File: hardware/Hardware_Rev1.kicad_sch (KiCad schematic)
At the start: 160 parts, among them J1 RJ45_LED_Shielded, J2 6P6C, Q1 BSS138, Q10 AO3401A, Q11 AO3401A, Q12 AO3401A, Q13 BSS138, Q14 BSS138, Q15 BSS138, Q16 AO3401A, Q17 AO3401A, Q18 AO3401A, Q19 BSS138, Q2 BSS138, Q20 BSS138, Q21 BSS138, Q22 AO3401A, Q23 AO3401A, Q24 AO3401A, Q3 BSS138, Q4 AO3401A, Q5 AO3401A, Q6 AO3401A, Q7 BSS138, Q8 BSS138, Q9 BSS138, U1 OKI, U2 Teensy4.1_DEV-16771

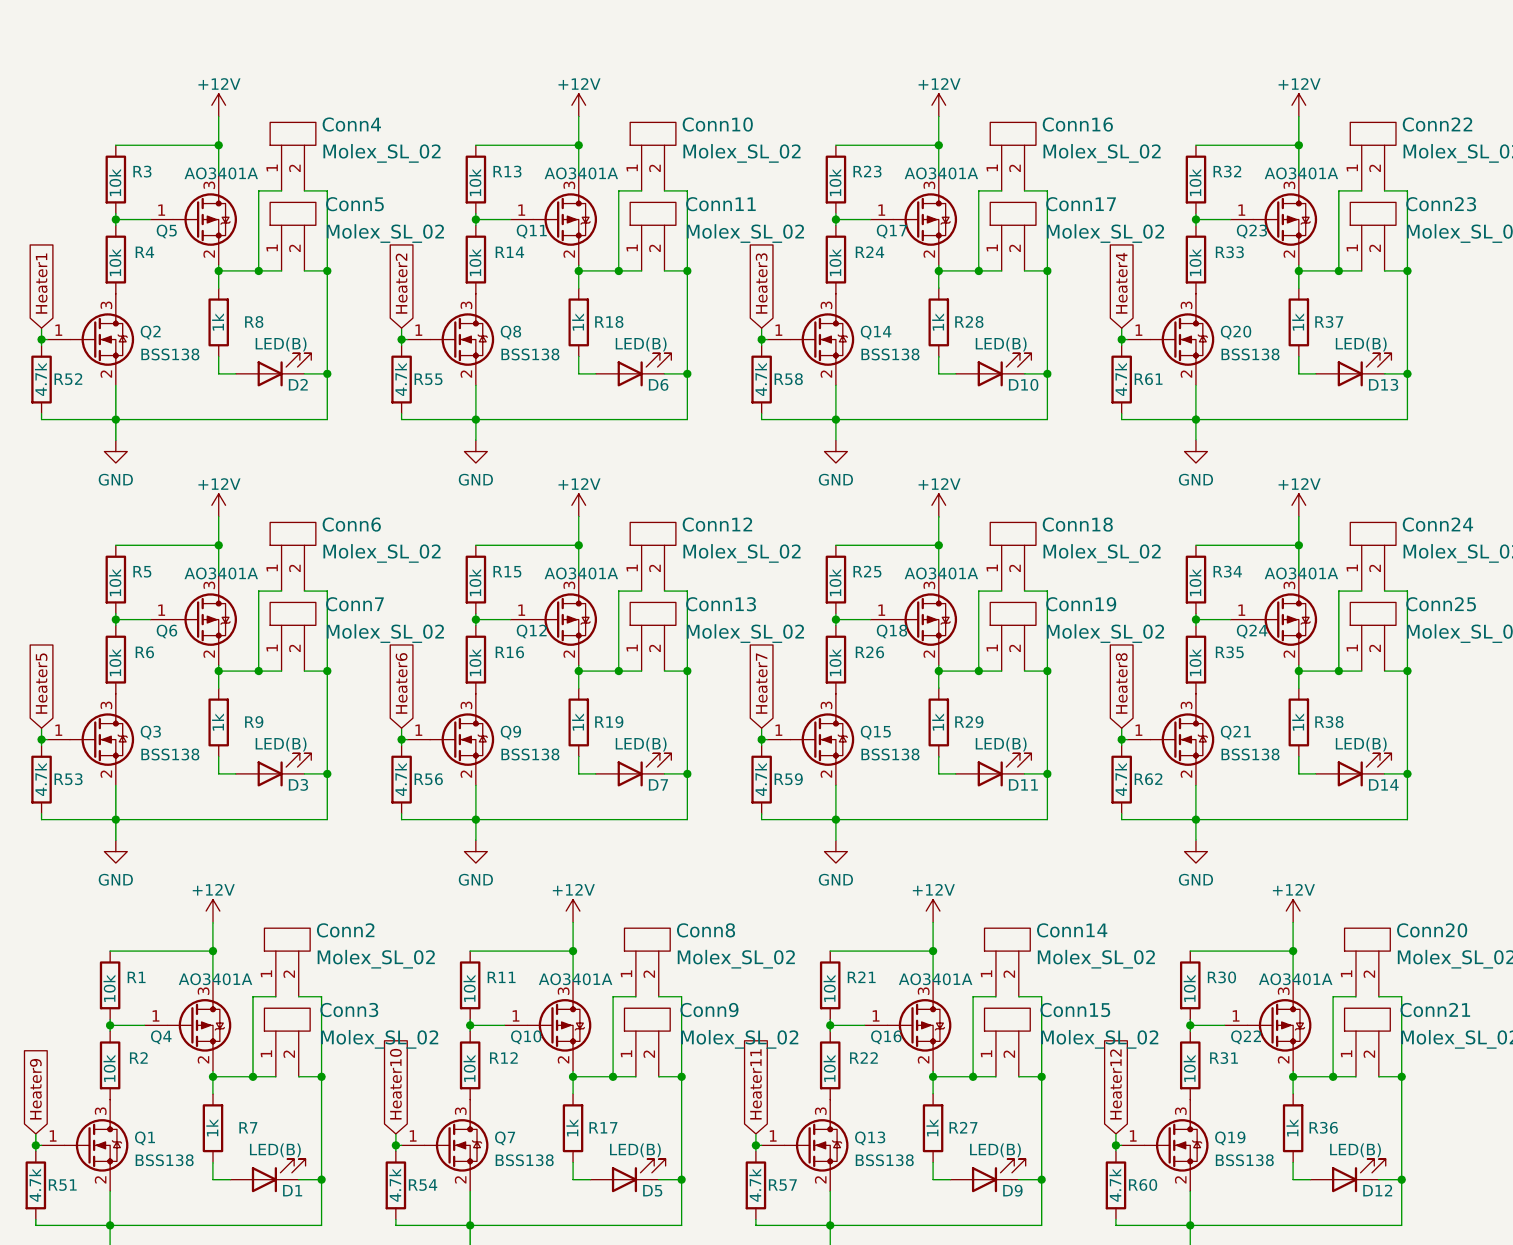
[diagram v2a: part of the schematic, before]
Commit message: Fixed schematic mosfets
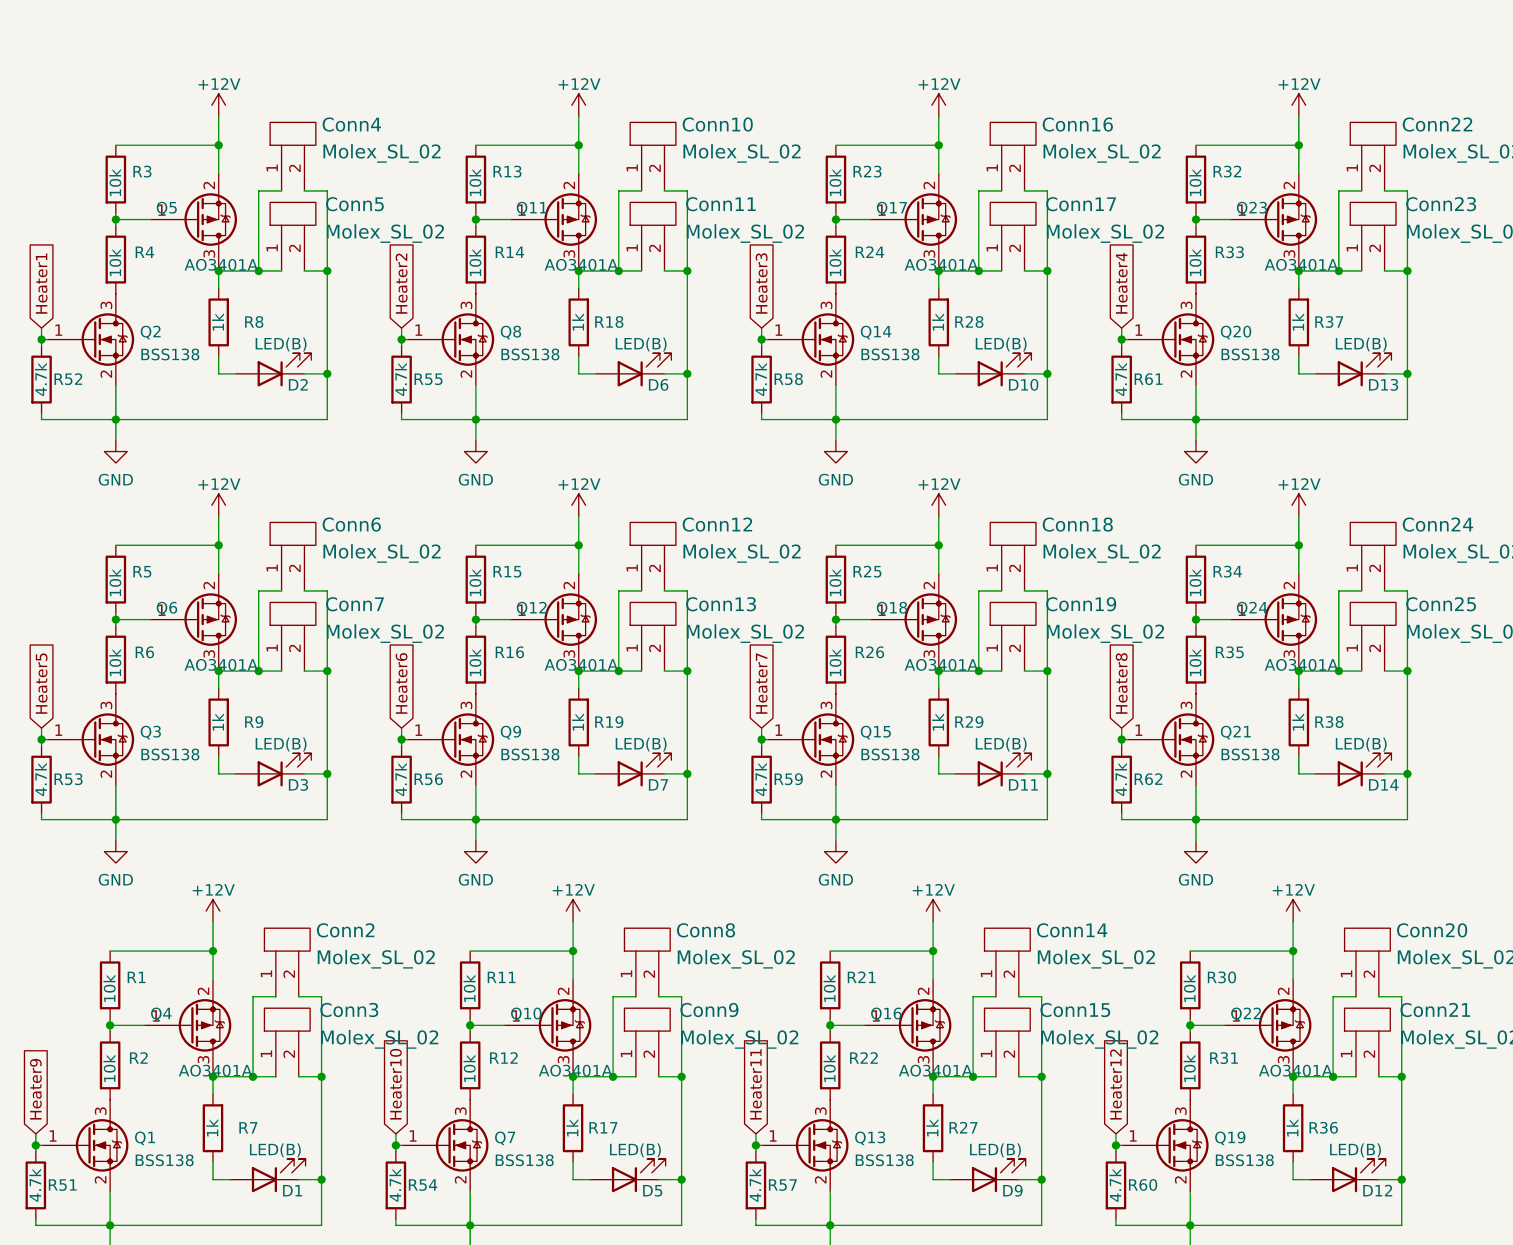
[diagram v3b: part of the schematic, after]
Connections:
- net +12V: now also Q10.2 (S), Q11.2 (S), Q12.2 (S), Q16.2 (S), Q17.2 (S), Q18.2 (S), Q22.2 (S), Q23.2 (S), Q24.2 (S), Q4.2 (S), Q5.2 (S), Q6.2 (S); no longer Q10.3 (D), Q11.3 (D), Q12.3 (D), Q16.3 (D), Q17.3 (D), Q18.3 (D), Q22.3 (D), Q23.3 (D), Q24.3 (D), Q4.3 (D), Q5.3 (D), Q6.3 (D)
- net at Conn20.1, Conn21.1, R36.2: now also Q22.3 (D); no longer Q22.2 (S)
- net at Conn22.1, Conn23.1, R37.2: now also Q23.3 (D); no longer Q23.2 (S)
- net at Conn8.1, Conn9.1, R17.2: now also Q10.3 (D); no longer Q10.2 (S)
- net at Conn4.1, Conn5.1, R8.2: now also Q5.3 (D); no longer Q5.2 (S)
- net at Conn14.1, Conn15.1, R27.2: now also Q16.3 (D); no longer Q16.2 (S)
- net at Conn6.1, Conn7.1, R9.2: now also Q6.3 (D); no longer Q6.2 (S)
- net at Conn12.1, Conn13.1, R19.2: now also Q12.3 (D); no longer Q12.2 (S)
- net at Conn16.1, Conn17.1, R28.2: now also Q17.3 (D); no longer Q17.2 (S)
- net at Conn24.1, Conn25.1, R38.2: now also Q24.3 (D); no longer Q24.2 (S)
- net at Conn10.1, Conn11.1, R18.2: now also Q11.3 (D); no longer Q11.2 (S)
- net at Conn2.1, Conn3.1, R7.2: now also Q4.3 (D); no longer Q4.2 (S)
- net at Conn18.1, Conn19.1, R29.2: now also Q18.3 (D); no longer Q18.2 (S)
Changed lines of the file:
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@@
     (pin "2")
   )
-  (symbol (lib_id "Transistor_FET:AO3401A") (at 150.495 161.29 0) (unit 1)
+  (symbol (lib_id "Transistor_FET:AO3401A") (at 150.495 161.29 0) (mirror x) (unit 1)
     (in_bom yes) (on_board yes)
-    (property "Reference" "Q22" (id 0) (at 146.05 162.56 0)
+    (property "Reference" "Q22" (id 0) (at 146.05 160.02 0)
       (effects (font (size 1.27 1.27)) (justify left))
     )
-    (property "Value" "AO3401A" (id 1) (at 149.225 156.21 0)
+    (property "Value" "AO3401A" (id 1) (at 149.225 166.37 0)
       (effects (font (size 1.27 1.27)) (justify left))
     )
-    (property "Footprint" "Package_TO_SOT_SMD:SOT-23" (id 2) (at 155.575 163.195 0)
+    (property "Footprint" "Package_TO_SOT_SMD:SOT-23" (id 2) (at 155.575 159.385 0)
       (effects (font (size 1.27 1.27) italic) (justify left) hide)
     )
@@
     (pin "3")
   )
-  (symbol (lib_id "Transistor_FET:AO3401A") (at 31.115 71.755 0) (unit 1)
+  (symbol (lib_id "Transistor_FET:AO3401A") (at 31.115 71.755 0) (mirror x) (unit 1)
     (in_bom yes) (on_board yes)
-    (property "Reference" "Q5" (id 0) (at 26.67 73.025 0)
+    (property "Reference" "Q5" (id 0) (at 26.67 70.485 0)
       (effects (font (size 1.27 1.27)) (justify left))
     )
-    (property "Value" "AO3401A" (id 1) (at 29.845 66.675 0)
+    (property "Value" "AO3401A" (id 1) (at 29.845 76.835 0)
       (effects (font (size 1.27 1.27)) (justify left))
     )
-    (property "Footprint" "Package_TO_SOT_SMD:SOT-23" (id 2) (at 36.195 73.66 0)
+    (property "Footprint" "Package_TO_SOT_SMD:SOT-23" (id 2) (at 36.195 69.85 0)
       (effects (font (size 1.27 1.27) italic) (justify left) hide)
     )
@@
     (pin "1")
   )
-  (symbol (lib_id "Transistor_FET:AO3401A") (at 31.115 116.205 0) (unit 1)
+  (symbol (lib_id "Transistor_FET:AO3401A") (at 31.115 116.205 0) (mirror x) (unit 1)
     (in_bom yes) (on_board yes)
-    (property "Reference" "Q6" (id 0) (at 26.67 117.475 0)
+    (property "Reference" "Q6" (id 0) (at 26.67 114.935 0)
       (effects (font (size 1.27 1.27)) (justify left))
     )
-    (property "Value" "AO3401A" (id 1) (at 29.845 111.125 0)
+    (property "Value" "AO3401A" (id 1) (at 29.845 121.285 0)
       (effects (font (size 1.27 1.27)) (justify left))
     )
-    (property "Footprint" "Package_TO_SOT_SMD:SOT-23" (id 2) (at 36.195 118.11 0)
+    (property "Footprint" "Package_TO_SOT_SMD:SOT-23" (id 2) (at 36.195 114.3 0)
       (effects (font (size 1.27 1.27) italic) (justify left) hide)
     )
@@
     (pin "2")
   )
-  (symbol (lib_id "Transistor_FET:AO3401A") (at 111.125 71.755 0) (unit 1)
+  (symbol (lib_id "Transistor_FET:AO3401A") (at 111.125 71.755 0) (mirror x) (unit 1)
     (in_bom yes) (on_board yes)
-    (property "Reference" "Q17" (id 0) (at 106.68 73.025 0)
+    (property "Reference" "Q17" (id 0) (at 106.68 70.485 0)
       (effects (font (size 1.27 1.27)) (justify left))
     )
-    (property "Value" "AO3401A" (id 1) (at 109.855 66.675 0)
+    (property "Value" "AO3401A" (id 1) (at 109.855 76.835 0)
       (effects (font (size 1.27 1.27)) (justify left))
     )
-    (property "Footprint" "Package_TO_SOT_SMD:SOT-23" (id 2) (at 116.205 73.66 0)
+    (property "Footprint" "Package_TO_SOT_SMD:SOT-23" (id 2) (at 116.205 69.85 0)
       (effects (font (size 1.27 1.27) italic) (justify left) hide)
     )
@@
     (pin "2")
   )
-  (symbol (lib_id "Transistor_FET:AO3401A") (at 110.49 161.29 0) (unit 1)
+  (symbol (lib_id "Transistor_FET:AO3401A") (at 110.49 161.29 0) (mirror x) (unit 1)
     (in_bom yes) (on_board yes)
-    (property "Reference" "Q16" (id 0) (at 106.045 162.56 0)
+    (property "Reference" "Q16" (id 0) (at 106.045 160.02 0)
       (effects (font (size 1.27 1.27)) (justify left))
     )
-    (property "Value" "AO3401A" (id 1) (at 109.22 156.21 0)
+    (property "Value" "AO3401A" (id 1) (at 109.22 166.37 0)
       (effects (font (size 1.27 1.27)) (justify left))
     )
-    (property "Footprint" "Package_TO_SOT_SMD:SOT-23" (id 2) (at 115.57 163.195 0)
+    (property "Footprint" "Package_TO_SOT_SMD:SOT-23" (id 2) (at 115.57 159.385 0)
       (effects (font (size 1.27 1.27) italic) (justify left) hide)
     )
@@
     (pin "2")
   )
-  (symbol (lib_id "Transistor_FET:AO3401A") (at 151.13 116.205 0) (unit 1)
+  (symbol (lib_id "Transistor_FET:AO3401A") (at 151.13 116.205 0) (mirror x) (unit 1)
     (in_bom yes) (on_board yes)
-    (property "Reference" "Q24" (id 0) (at 146.685 117.475 0)
+    (property "Reference" "Q24" (id 0) (at 146.685 114.935 0)
       (effects (font (size 1.27 1.27)) (justify left))
     )
-    (property "Value" "AO3401A" (id 1) (at 149.86 111.125 0)
+    (property "Value" "AO3401A" (id 1) (at 149.86 121.285 0)
       (effects (font (size 1.27 1.27)) (justify left))
     )
-    (property "Footprint" "Package_TO_SOT_SMD:SOT-23" (id 2) (at 156.21 118.11 0)
+    (property "Footprint" "Package_TO_SOT_SMD:SOT-23" (id 2) (at 156.21 114.3 0)
       (effects (font (size 1.27 1.27) italic) (justify left) hide)
     )
@@
     (pin "2")
   )
-  (symbol (lib_id "Transistor_FET:AO3401A") (at 70.485 161.29 0) (unit 1)
+  (symbol (lib_id "Transistor_FET:AO3401A") (at 70.485 161.29 0) (mirror x) (unit 1)
     (in_bom yes) (on_board yes)
-    (property "Reference" "Q10" (id 0) (at 66.04 162.56 0)
+    (property "Reference" "Q10" (id 0) (at 66.04 160.02 0)
       (effects (font (size 1.27 1.27)) (justify left))
     )
-    (property "Value" "AO3401A" (id 1) (at 69.215 156.21 0)
+    (property "Value" "AO3401A" (id 1) (at 69.215 166.37 0)
       (effects (font (size 1.27 1.27)) (justify left))
     )
-    (property "Footprint" "Package_TO_SOT_SMD:SOT-23" (id 2) (at 75.565 163.195 0)
+    (property "Footprint" "Package_TO_SOT_SMD:SOT-23" (id 2) (at 75.565 159.385 0)
       (effects (font (size 1.27 1.27) italic) (justify left) hide)
     )
@@
     (pin "3")
   )
-  (symbol (lib_id "Transistor_FET:AO3401A") (at 71.12 116.205 0) (unit 1)
+  (symbol (lib_id "Transistor_FET:AO3401A") (at 71.12 116.205 0) (mirror x) (unit 1)
     (in_bom yes) (on_board yes)
-    (property "Reference" "Q12" (id 0) (at 66.675 117.475 0)
+    (property "Reference" "Q12" (id 0) (at 66.675 114.935 0)
       (effects (font (size 1.27 1.27)) (justify left))
     )
-    (property "Value" "AO3401A" (id 1) (at 69.85 111.125 0)
+    (property "Value" "AO3401A" (id 1) (at 69.85 121.285 0)
       (effects (font (size 1.27 1.27)) (justify left))
     )
-    (property "Footprint" "Package_TO_SOT_SMD:SOT-23" (id 2) (at 76.2 118.11 0)
+    (property "Footprint" "Package_TO_SOT_SMD:SOT-23" (id 2) (at 76.2 114.3 0)
       (effects (font (size 1.27 1.27) italic) (justify left) hide)
     )
@@
     (pin "1")
   )
-  (symbol (lib_id "Transistor_FET:AO3401A") (at 30.48 161.29 0) (unit 1)
+  (symbol (lib_id "Transistor_FET:AO3401A") (at 30.48 161.29 0) (mirror x) (unit 1)
     (in_bom yes) (on_board yes)
-    (property "Reference" "Q4" (id 0) (at 26.035 162.56 0)
+    (property "Reference" "Q4" (id 0) (at 26.035 160.02 0)
       (effects (font (size 1.27 1.27)) (justify left))
     )
-    (property "Value" "AO3401A" (id 1) (at 29.21 156.21 0)
+    (property "Value" "AO3401A" (id 1) (at 29.21 166.37 0)
       (effects (font (size 1.27 1.27)) (justify left))
     )
-    (property "Footprint" "Package_TO_SOT_SMD:SOT-23" (id 2) (at 35.56 163.195 0)
+    (property "Footprint" "Package_TO_SOT_SMD:SOT-23" (id 2) (at 35.56 159.385 0)
       (effects (font (size 1.27 1.27) italic) (justify left) hide)
     )
@@
     (pin "3")
   )
-  (symbol (lib_id "Transistor_FET:AO3401A") (at 111.125 116.205 0) (unit 1)
+  (symbol (lib_id "Transistor_FET:AO3401A") (at 111.125 116.205 0) (mirror x) (unit 1)
     (in_bom yes) (on_board yes)
-    (property "Reference" "Q18" (id 0) (at 106.68 117.475 0)
+    (property "Reference" "Q18" (id 0) (at 106.68 114.935 0)
       (effects (font (size 1.27 1.27)) (justify left))
     )
-    (property "Value" "AO3401A" (id 1) (at 109.855 111.125 0)
+    (property "Value" "AO3401A" (id 1) (at 109.855 121.285 0)
       (effects (font (size 1.27 1.27)) (justify left))
     )
-    (property "Footprint" "Package_TO_SOT_SMD:SOT-23" (id 2) (at 116.205 118.11 0)
+    (property "Footprint" "Package_TO_SOT_SMD:SOT-23" (id 2) (at 116.205 114.3 0)
       (effects (font (size 1.27 1.27) italic) (justify left) hide)
     )
@@
     (pin "2")
   )
-  (symbol (lib_id "Transistor_FET:AO3401A") (at 71.12 71.755 0) (unit 1)
+  (symbol (lib_id "Transistor_FET:AO3401A") (at 71.12 71.755 0) (mirror x) (unit 1)
     (in_bom yes) (on_board yes)
-    (property "Reference" "Q11" (id 0) (at 66.675 73.025 0)
+    (property "Reference" "Q11" (id 0) (at 66.675 70.485 0)
       (effects (font (size 1.27 1.27)) (justify left))
     )
-    (property "Value" "AO3401A" (id 1) (at 69.85 66.675 0)
+    (property "Value" "AO3401A" (id 1) (at 69.85 76.835 0)
       (effects (font (size 1.27 1.27)) (justify left))
     )
-    (property "Footprint" "Package_TO_SOT_SMD:SOT-23" (id 2) (at 76.2 73.66 0)
+    (property "Footprint" "Package_TO_SOT_SMD:SOT-23" (id 2) (at 76.2 69.85 0)
       (effects (font (size 1.27 1.27) italic) (justify left) hide)
     )
@@
     (pin "2")
   )
-  (symbol (lib_id "Transistor_FET:AO3401A") (at 151.13 71.755 0) (unit 1)
+  (symbol (lib_id "Transistor_FET:AO3401A") (at 151.13 71.755 0) (mirror x) (unit 1)
     (in_bom yes) (on_board yes)
-    (property "Reference" "Q23" (id 0) (at 146.685 73.025 0)
+    (property "Reference" "Q23" (id 0) (at 146.685 70.485 0)
       (effects (font (size 1.27 1.27)) (justify left))
     )
-    (property "Value" "AO3401A" (id 1) (at 149.86 66.675 0)
+    (property "Value" "AO3401A" (id 1) (at 149.86 76.835 0)
       (effects (font (size 1.27 1.27)) (justify left))
     )
-    (property "Footprint" "Package_TO_SOT_SMD:SOT-23" (id 2) (at 156.21 73.66 0)
+    (property "Footprint" "Package_TO_SOT_SMD:SOT-23" (id 2) (at 156.21 69.85 0)
       (effects (font (size 1.27 1.27) italic) (justify left) hide)
     )

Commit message: Rev2 schematic
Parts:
- removed Conn10, Conn11, Conn12, Conn13, Conn14, Conn15, Conn16, Conn17, Conn18, Conn19, Conn2, Conn20, Conn21, Conn22, Conn23, Conn24, Conn25, Conn3, Conn4, Conn5, Conn6, Conn7, Conn8, Conn9: Molex_SL_02, MRDT_Connectors:MOLEX_SL_02_Vertical, symbol MRDT_Connectors:Molex_SL_02
- removed J2: 6P6C, Connector_PinHeader_2.00mm:PinHeader_2x03_P2.00mm_Vertical, symbol Connector:6P6C
- removed Q10, Q11, Q12, Q16, Q17, Q18, Q22, Q23, Q24, Q4, Q5, Q6: AO3401A, Package_TO_SOT_SMD:SOT-23, symbol Transistor_FET:AO3401A
- added C4: 100uF, Capacitor_THT:CP_Radial_D6.3mm_P2.50mm, symbol Device:C_Polarized
- added C5: 220uF, Capacitor_THT:CP_Radial_D6.3mm_P2.50mm, symbol Device:C_Polarized
- added C6: 470uF, Capacitor_THT:CP_Radial_D10.0mm_P2.50mm, symbol Device:C_Polarized
- added Conn10, Conn11, Conn12, Conn13, Conn2, Conn3, Conn4, Conn5, Conn6, Conn7, Conn8, Conn9: AndersonPP, MRDT_Connectors:Square_Anderson_2_V_Side_By_Side, symbol MRDT_Connectors:AndersonPP
- added Q10, Q11, Q12, Q16, Q17, Q18, Q22, Q23, Q24, Q4, Q5, Q6: Q_PMOS_GSD, Package_TO_SOT_SMD:SOT-23-3, symbol Device:Q_PMOS_GSD
- U2: footprint MRDT_Shields:Teensy_4_1_Bare -> MRDT_Shields:Teensy_4_1_Ethernet
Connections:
- net RX+ is gone; now on net R+: J1.4
- net RX- is gone; now on net R-: J1.6
- net TX+ is gone; now on net T+: J1.1
- net TX- is gone; now on net T-: J1.3
- net +12V: now also C4.1, C5.1, C6.1, Q10.3 (D), Q11.3 (D), Q12.3 (D), Q16.3 (D), Q17.3 (D), Q18.3 (D), Q22.3 (D), Q23.3 (D), Q24.3 (D), Q4.3 (D), Q5.3 (D), Q6.3 (D)
- net GND: now also C3.2, J1.8, J1.9, C4.2, C5.2, C6.2, Conn10.1 (GND), Conn11.1 (GND), Conn12.1 (GND), Conn13.1 (GND), Conn2.1 (GND), Conn3.1 (GND), Conn4.1 (GND), Conn5.1 (GND), Conn6.1 (GND), Conn7.1 (GND), Conn8.1 (GND), Conn9.1 (GND)
- net at R34.2, R35.1: now also Q24.1 (G)
- net at R30.2, R31.1: now also Q22.1 (G)
- net at R36.2: now also Conn13.1, Q22.2 (S)
- net at R21.2, R22.1: now also Q17.1 (G)
- net Overheat2: now reaches R40.2, U2.8 (TX2)
- net LED: now reaches J1.10
- net LED: now also U2.LED
- net Overheat10: now reaches R48.2, U2.0 (RX1)
- net Overheat9: now reaches R47.2, U2.1 (TX1)
- net Overheat8: now reaches R46.2, U2.2 (OUT2)
- net Overheat11: now reaches R49.2, U2.22 (A8)
- net Overheat12: now reaches R50.2, U2.23 (A9)
- net Overheat7: now reaches R45.2, U2.3 (LRCLK2)
- net Overheat6: now reaches R44.2, U2.4 (BCLK2)
- net Overheat5: now reaches R43.2, U2.5 (IN2)
- net Overheat4: now reaches R42.2, U2.6 (OUT1D)
- net Overheat3: now reaches R41.2, U2.7 (RX2)
- net Overheat1: now reaches R39.2, U2.9 (OUT1C)
- net R-: now reaches U2.R (R-)
- net R+: now reaches U2.R+
- net T-: now reaches U2.T (T-)
- net T+: now reaches U2.T+
- net at R15.2, R16.1: now also Q12.1 (G)
- net at R37.2: now also Conn11.1, Q23.2 (S)
- net at R17.2: now also Conn7.1, Q10.2 (S)
- net at R3.2, R4.1: now also Q5.1 (G)
- net at R8.2: now also Conn2.1, Q5.2 (S)
- net at R27.2: now also Conn10.1, Q17.2 (S)
- net at R5.2, R6.1: now also Q6.1 (G)
- net at R9.2: now also Conn3.1, Q6.2 (S)
- net at R1.2, R2.1: now also Q4.1 (G)
- net at R19.2: now also Conn6.1, Q12.2 (S)
- net at R23.2, R24.1: now also Q16.1 (G)
- net at R28.2: now also Conn8.1, Q16.2 (S)
- net at R32.2, R33.1: now also Q23.1 (G)
- net at R25.2, R26.1: now also Q18.1 (G)
- net at R38.2: now also Conn12.1, Q24.2 (S)
- net at R11.2, R12.1: now also Q10.1 (G)
- net at R18.2: now also Conn5.1, Q11.2 (S)
- net at R7.2: now also Conn4.1, Q4.2 (S)
- net at R13.2, R14.1: now also Q11.1 (G)
- net at R29.2: now also Conn9.1, Q18.2 (S)
- no-connect marks 22 -> 17
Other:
- moved on the sheet: C1, C2, Conn1A, Conn1B, D10, D15, D16, D17, D18, D19, D2, D20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
